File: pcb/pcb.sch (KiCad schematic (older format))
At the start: 42 parts, among them CN1 USBA_FEMALE, CN4 MicroUSB, T1 MMUN2133LT1G, U1 TPS61090RSAR, U2 MCP73871, X1 TERMBLOCK_1X2

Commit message: excluding unused kicad files, added start of schematic with reference
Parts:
- removed FID1, FID2, FID3: FIDUCIAL\"\", pcb:FIDUCIAL_1MM, symbol pcb-eagle-import:FIDUCIAL""
- removed U$10, U$11: MOUNTINGHOLE2.5, pcb:MOUNTINGHOLE_2.5_PLATED, symbol pcb-eagle-import:MOUNTINGHOLE2.5
- added C1, C2: 10µF, lipousbc:0805-NO@1, symbol lipousbc-eagle-import:CAP_CERAMIC0805-NOOUTLINE
- added C?: 10 uF, symbol Device:C
- added CN2: JSTPH, lipousbc:JSTPH2, symbol lipousbc-eagle-import:JST_2PIN
- added D?: ORANGE_LED, symbol Device:LED
- added D?: GREEN_LED, symbol Device:LED
- added J?: B2B-PH-K-S_LF__SN_, digikey-footprints:PinHeader_1x2_P2mm_Drill1mm, symbol dk_Rectangular-Connectors-Headers-Male-Pins:B2B-PH-K-S_LF__SN_
- added J?: Conn_02x08_Odd_Even, Connector_PinHeader_2.54mm:PinHeader_2x08_P2.54mm_Vertical, symbol Connector_Generic:Conn_02x08_Odd_Even
- added JP4: HEADER-1X570MIL, lipousbc:1X05_ROUND_70, symbol lipousbc-eagle-import:HEADER-1X570MIL
- added LED1: RED, lipousbc:CHIPLED_0805_NOOUTLINE, symbol lipousbc-eagle-import:LED0805_NOOUTLINE
- added LED2: GREEN, lipousbc:CHIPLED_0805_NOOUTLINE, symbol lipousbc-eagle-import:LED0805_NOOUTLINE
- added R1, R2: 470, lipousbc:0603-NO, symbol lipousbc-eagle-import:RESISTOR_0603_NOOUT
- added R3: 10K\\, lipousbc:0603-NO, symbol lipousbc-eagle-import:RESISTOR_0603_NOOUT
- added R4: 2.2K, lipousbc:0603-NO, symbol lipousbc-eagle-import:RESISTOR_0603_NOOUT
- added R5, R6: 5.1K, lipousbc:0603-NO, symbol lipousbc-eagle-import:RESISTOR_0603_NOOUT
- added R? (x2): 5.1k, symbol Device:R
- added R?: 270K, symbol Device:R
- added R? (x2): 100K, symbol Device:R
- added R?: 1.0K, symbol Device:R
- added R? (x2): 1K, symbol Device:R
- added S?: GPTS203211B, digikey-footprints:PushButton_12x12mm_THT_GPTS203211B, symbol dk_Pushbutton-Switches:GPTS203211B
- added SJ1: SOLDERJUMPER, lipousbc:SOLDERJUMPER_ARROW_NOPASTE, symbol lipousbc-eagle-import:SOLDERJUMPER
- added TH?: 15K, symbol Device:Thermistor
- added U1: MCP73831T-2ACI/OT, lipousbc:SOT23-5, symbol lipousbc-eagle-import:MCP73831_2
- added U?: TPS61090, Package_DFN_QFN:Texas_S-PVQFN-N16_EP2.7x2.7mm_ThermalVias, symbol Regulator_Switching:TPS61090
- added U?: MCP73871-1AA, Package_DFN_QFN:QFN-20-1EP_4x4mm_P0.5mm_EP2.5x2.5mm, symbol Battery_Management:MCP73871-1AA
- added X2: USB_C, lipousbc:USB_C_CUSB31-CFM2AX-01-X, symbol lipousbc-eagle-import:USB_C
- added X?: USB_C, digikey-footprints:USB-C_Female_E8124-015-01, symbol lipousbc-eagle-import:USB_C
- B1: symbol pcb-eagle-import:BATTERY -> pcb-rescue:BATTERY-pcb-eagle-import
- C6: symbol pcb-eagle-import:C-USC1210 -> pcb-rescue:C-USC1210-pcb-eagle-import
- CN1: symbol pcb-eagle-import:USB_TYPEAPTHFML -> pcb-rescue:USB_TYPEAPTHFML-pcb-eagle-import
- CN4: symbol pcb-eagle-import:USBMICRO_20329 -> pcb-rescue:USBMICRO_20329-pcb-eagle-import
- JP2: symbol pcb-eagle-import:HEADER-1X8ROUND -> pcb-rescue:HEADER-1X8ROUND-pcb-eagle-import
- L1: symbol pcb-eagle-import:INDUCTORTDK_VLC5045 -> pcb-rescue:INDUCTORTDK_VLC5045-pcb-eagle-import
- T1: symbol pcb-eagle-import:-PNP_DRIVER-SC59-BEC -> pcb-rescue:-PNP_DRIVER-SC59-BEC-pcb-eagle-import
- U1: symbol pcb-eagle-import:VREG_TPS6103X -> pcb-rescue:VREG_TPS6103X-pcb-eagle-import
- U2: symbol pcb-eagle-import:MCP73871 -> pcb-rescue:MCP73871-pcb-eagle-import
- X1: symbol pcb-eagle-import:TERMBLOCK_1X2 -> pcb-rescue:TERMBLOCK_1X2-pcb-eagle-import
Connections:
- net labels added: 5V, CC1, CC2, D+, D-
- net labels removed: FRAME_A4_ADAFRUIT
- wire segments 129 -> 205
- no-connect marks 0 -> 5
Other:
- note added: "10K = 100mA"
- note added: "5.0K = 200mA"
- note added: "Input power over micro-USB"
- note added: "Output power over USB-A"
- note added: "REFERENCE: Adafruit Micro-Lipo Charger\n(https://github.com/adafruit/Adafruit-MicroLipo-PCB)"
- note added: "REFERENCE: Adafruit PowerBoost 1000C\n(https://github.com/adafruit/Adafruit-PowerBoost-1000C)"
- note added: "RPi header, first 16 pins (2x8)"
- note added: "Set to UFP (Peripheral)\nAlso marks this as a USB 2.0 peripheral device\n\nFor DFP (Host) you need pullups\nhere instead of pulldowns."
- note added: "Upstream/Downstream Facing Port Setup:"
- moved on the sheet: C1, C2, C4, C7, C8, CHRG/LBO1, DONE1, LED1, LED2, R1, R10, R11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

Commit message: added some more components
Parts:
- added C?: 10 uF, symbol Device:C
- added Q?: MMUN2211LT1G, digikey-footprints:SOT-23-3, symbol dk_Transistors-Bipolar-BJT-Single-Pre-Biased:MMUN2211LT1G
- C1, C2: symbol lipousbc-eagle-import:CAP_CERAMIC0805-NOOUTLINE -> pcb-rescue:CAP_CERAMIC0805-NOOUTLINE-lipousbc-eagle-import
- CN2: symbol lipousbc-eagle-import:JST_2PIN -> pcb-rescue:JST_2PIN-lipousbc-eagle-import
- JP4: symbol lipousbc-eagle-import:HEADER-1X570MIL -> pcb-rescue:HEADER-1X570MIL-lipousbc-eagle-import
- LED1, LED2: symbol lipousbc-eagle-import:LED0805_NOOUTLINE -> pcb-rescue:LED0805_NOOUTLINE-lipousbc-eagle-import
- R1, R2, R3, R4, R5, R6: symbol lipousbc-eagle-import:RESISTOR_0603_NOOUT -> pcb-rescue:RESISTOR_0603_NOOUT-lipousbc-eagle-import
- SJ1: symbol lipousbc-eagle-import:SOLDERJUMPER -> pcb-rescue:SOLDERJUMPER-lipousbc-eagle-import
- U1: symbol lipousbc-eagle-import:MCP73831_2 -> pcb-rescue:MCP73831_2-lipousbc-eagle-import
- X2, X?: symbol lipousbc-eagle-import:USB_C -> pcb-rescue:USB_C-lipousbc-eagle-import
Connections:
- net labels added: PI_3V3, PI_BCM_14_TXD, PI_BCM_15_RXD, PI_BCM_17, PI_BCM_18_PWM0, PI_BCM_22, PI_BCM_23, PI_BCM_27, PI_BCM_2_SDA, PI_BCM_3_SCL, PI_BCM_4_GPCLK0
- wire segments 205 -> 212
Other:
- moved on the sheet: J?, S?

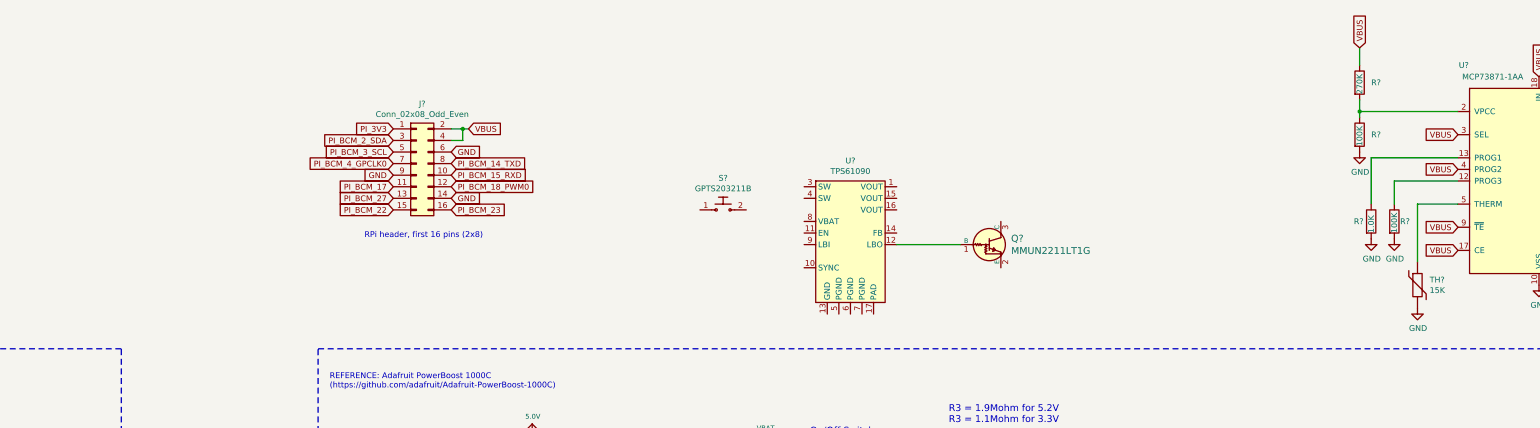
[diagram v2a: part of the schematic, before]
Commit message: first pass of schematic complete
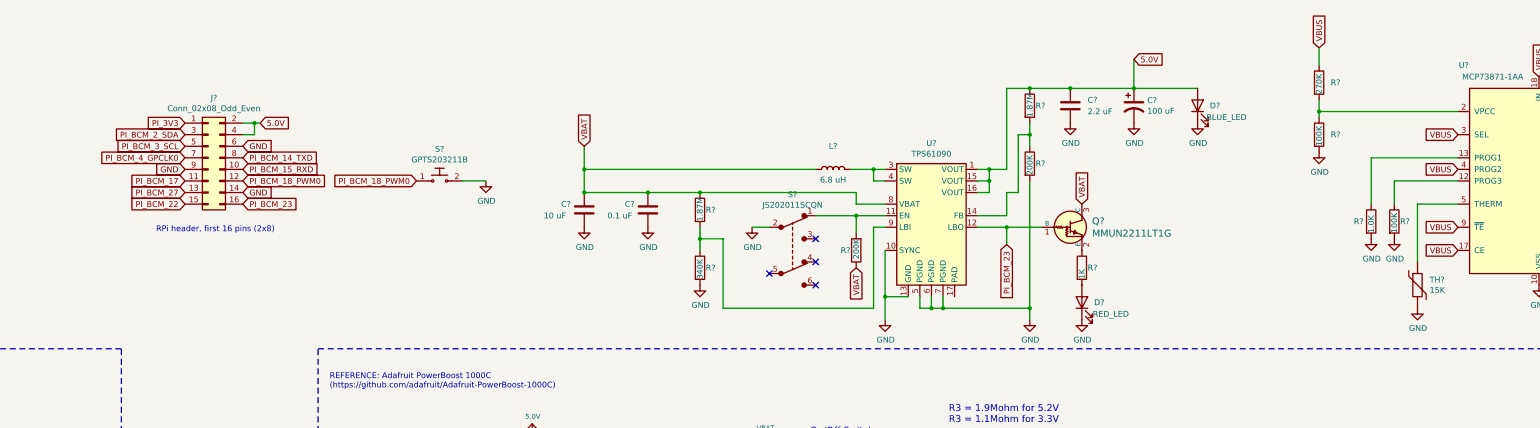
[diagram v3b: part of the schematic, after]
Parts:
- added C?: 2.2 uF, symbol Device:C
- added C?: 100 uF, symbol Device:CP1
- added C?: 10 uF, symbol Device:C
- added C?: 0.1 uF, symbol Device:C
- added D?: RED_LED, symbol Device:LED
- added D?: BLUE_LED, symbol Device:LED
- added L?: 6.8 uH, symbol Device:L
- added R? (x2): 200K, symbol Device:R
- added R?: 1K, symbol Device:R
- added R? (x2): 1.87M, symbol Device:R
- added R?: 340K, symbol Device:R
- added S?: JS202011SCQN, Button_Switch_THT:SW_CuK_JS202011AQN_DPDT_Angled, symbol dk_Slide-Switches:JS202011SCQN
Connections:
- net 5.0V: now also J?.2 (Pin_2), J?.4 (Pin_4), U?.1 (VOUT), U?.15 (VOUT), U?.16 (VOUT), C?.1, C?.1, D?.2 (A), R?.1
- net GND: now also S?.2, U?.10 (SYNC), U?.13 (GND), U?.5 (PGND), U?.6 (PGND), U?.7 (PGND), C?.2, C?.2, C?.2, C?.2, D?.1 (K), D?.1 (K), R?.2, R?.2, S?.2
- net PI_BCM_18_PWM0: now also S?.1
- net PI_BCM_23: now also Q?.1 (B), U?.12 (LBO)
- net VBAT: now also Q?.3 (C), U?.8 (VBAT), C?.1, C?.1, L?.1, R?.1, R?.1
- net VBUS: no longer J?.2 (Pin_2), J?.4 (Pin_4)
- net at Q?.2 (E): now also R?.1
- net at U?.11 (EN): now also R?.2, S?.1
- net at U?.14 (FB): now also R?.1, R?.2
- net at U?.3 (SW): now also U?.4 (SW), L?.2
- net at U?.9 (LBI): now also R?.1, R?.2
- new net: D?.2 (A), R?.2
- no-connect marks 5 -> 9
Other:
- moved on the sheet: J?, Q?, R?, S?, U?

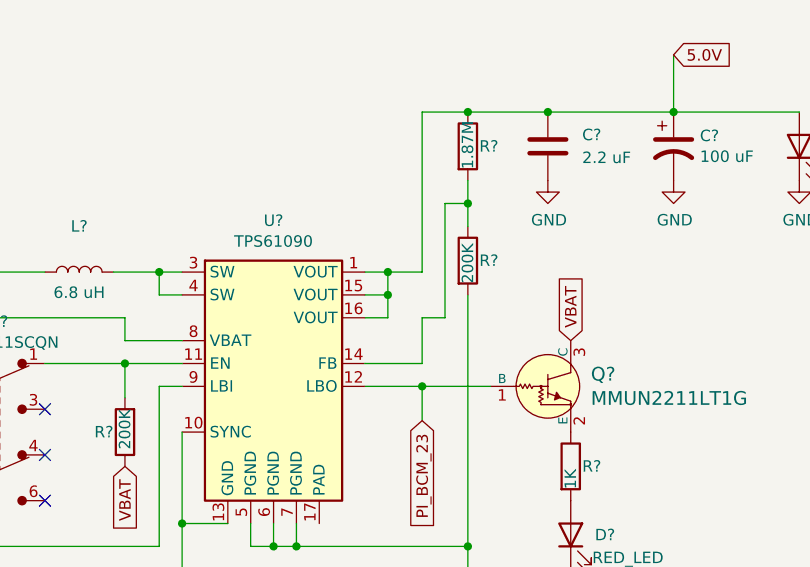
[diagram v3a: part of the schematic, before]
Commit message: updated schematic a bit, going to delete reference
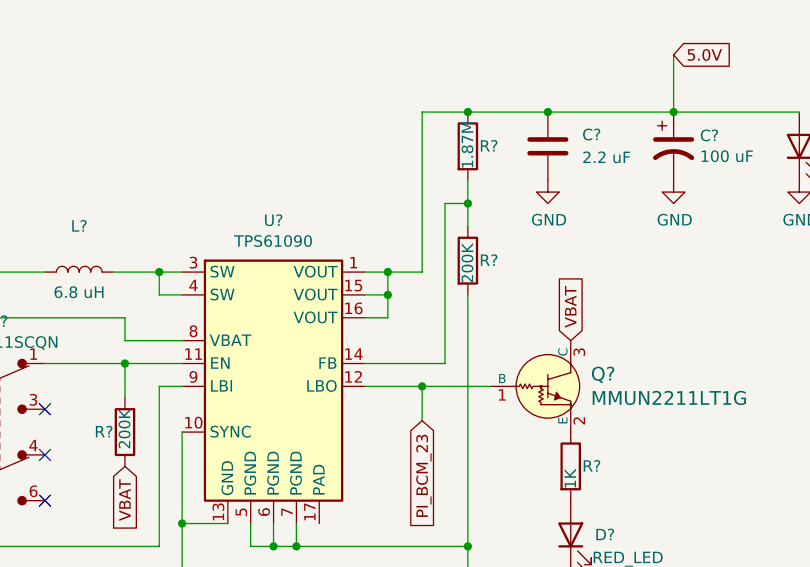
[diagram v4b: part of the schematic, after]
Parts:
- C? (x3): footprint (none) -> Capacitor_SMD:C_0805_2012Metric
- C?: footprint (none) -> Capacitor_SMD:C_0201_0603Metric
- C?: footprint (none) -> Capacitor_SMD:C_1206_3216Metric
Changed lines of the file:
@@
 F 0 "C?" H 9050 10900 50  0000 L CNN
 F 1 "10 uF" H 8950 10800 50  0000 L CNN
-F 2 "" H 9338 10650 50  0001 C CNN
+F 2 "Capacitor_SMD:C_0805_2012Metric" H 9338 10650 50  0001 C CNN
 F 3 "~" H 9300 10800 50  0001 C CNN
 	1    9300 10800
@@
 F 0 "C?" H 25950 11150 50  0000 L CNN
 F 1 "10 uF" H 25850 11050 50  0000 L CNN
-F 2 "" H 26238 10900 50  0001 C CNN
+F 2 "Capacitor_SMD:C_0805_2012Metric" H 26238 10900 50  0001 C CNN
 F 3 "~" H 26200 11050 50  0001 C CNN
 	1    26200 11050
@@
 	19200 11200 19300 11200
 Wire Wire Line
-	20100 11500 20350 11500
-Wire Wire Line
-	20350 11500 20350 11300
-Wire Wire Line
 	20200 11100 20200 11200
 Wire Wire Line
@@
 	20350 10400 20550 10400
 Wire Wire Line
-	20350 11300 20450 11300
-Wire Wire Line
-	20450 11300 20450 10800
-Wire Wire Line
 	20450 10800 20550 10800
 Wire Wire Line
@@
 F 0 "C?" H 21050 10600 50  0000 L CNN
 F 1 "2.2 uF" H 21050 10500 50  0000 L CNN
-F 2 "" H 20938 10400 50  0001 C CNN
-F 3 "~" H 20900 10550 50  0001 C CNN
+F 2 "Capacitor_SMD:C_0201_0603Metric" H 20938 10400 50  0001 C CNN
+F 3 "https://www.digikey.com/product-detail/en/C0603C225M9PAC7867/399-13137-1-ND/5879291/?itemSeq=336152622" H 20900 10550 50  0001 C CNN
 	1    20900 10550
 	1    0    0    -1
@@
 F 0 "C?" H 21565 10596 50  0000 L CNN
 F 1 "100 uF" H 21565 10505 50  0000 L CNN
-F 2 "" H 21450 10550 50  0001 C CNN
-F 3 "~" H 21450 10550 50  0001 C CNN
+F 2 "Capacitor_SMD:C_1206_3216Metric" H 21450 10550 50  0001 C CNN
+F 3 "https://www.digikey.com/product-detail/en/kemet/C1206C107M9PACTU/399-5620-1-ND/2057834" H 21450 10550 50  0001 C CNN
 	1    21450 10550
 	1    0    0    -1
@@
 F 0 "C?" H 16500 11500 50  0000 L CNN
 F 1 "10 uF" H 16350 11400 50  0000 L CNN
-F 2 "" H 16738 11300 50  0001 C CNN
+F 2 "Capacitor_SMD:C_0805_2012Metric" H 16738 11300 50  0001 C CNN
 F 3 "~" H 16700 11450 50  0001 C CNN
 	1    16700 11450
@@
 Wire Wire Line
 	23050 10600 24250 10600
+Wire Wire Line
+	20100 11500 20450 11500
+Wire Wire Line
+	20450 10800 20450 11500
 $EndSCHEMATC

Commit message: netlist has a bug it seems
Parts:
- removed B1: JST 2-PH, pcb:JSTPH2, symbol pcb-rescue:BATTERY-pcb-eagle-import
- removed C1, C2: 10µF, lipousbc:0805-NO@1, symbol pcb-rescue:CAP_CERAMIC0805-NOOUTLINE-lipousbc-eagle-import
- removed C1, C7, C8: 10uF, pcb:0805-NO, symbol pcb-eagle-import:CAP_CERAMIC0805-NOOUTLINE
- removed C2: 2.2uF, pcb:0805-NO, symbol pcb-eagle-import:CAP_CERAMIC0805-NOOUTLINE
- removed C4: 0.1uF, pcb:0805_10MGAP, symbol pcb-eagle-import:CAP_CERAMIC0805_10MGAP
- removed C6: 100uF, pcb:C1210, symbol pcb-rescue:C-USC1210-pcb-eagle-import
- removed CHRG/LBO1: ORANGE, pcb:CHIPLED_0805_NOOUTLINE, symbol pcb-eagle-import:LED0805_NOOUTLINE
- removed CN1: USBA_FEMALE, pcb:USB_HOST-PTH, symbol pcb-rescue:USB_TYPEAPTHFML-pcb-eagle-import
- removed CN2: JSTPH, lipousbc:JSTPH2, symbol pcb-rescue:JST_2PIN-lipousbc-eagle-import
- removed CN4: MicroUSB, pcb:4UCONN_20329, symbol pcb-rescue:USBMICRO_20329-pcb-eagle-import
- removed DONE1: GREEN, pcb:CHIPLED_0805_NOOUTLINE, symbol pcb-eagle-import:LED0805_NOOUTLINE
- removed JP2: HEADER-1X8ROUND, pcb:1X08_ROUND, symbol pcb-rescue:HEADER-1X8ROUND-pcb-eagle-import
- removed JP4: HEADER-1X570MIL, lipousbc:1X05_ROUND_70, symbol pcb-rescue:HEADER-1X570MIL-lipousbc-eagle-import
- removed L1: 6.8uH, pcb:INDUCTOR_5X5MM_TDK_VLC5045, symbol pcb-rescue:INDUCTORTDK_VLC5045-pcb-eagle-import
- removed LED1: RED, lipousbc:CHIPLED_0805_NOOUTLINE, symbol pcb-rescue:LED0805_NOOUTLINE-lipousbc-eagle-import
- removed LED1: RED, pcb:CHIPLED_0805_NOOUTLINE, symbol pcb-eagle-import:LED0805_NOOUTLINE
- removed LED2: GREEN, lipousbc:CHIPLED_0805_NOOUTLINE, symbol pcb-rescue:LED0805_NOOUTLINE-lipousbc-eagle-import
- removed LED2: BLUE, pcb:CHIPLED_0805_NOOUTLINE, symbol pcb-eagle-import:LED0805_NOOUTLINE
- removed R1, R2: 470, lipousbc:0603-NO, symbol pcb-rescue:RESISTOR_0603_NOOUT-lipousbc-eagle-import
- removed R1: 1.87M, pcb:_0805MP, symbol pcb-eagle-import:RESISTOR_0805MP
- removed R10: 49.9K, pcb:0805-NO, symbol pcb-eagle-import:RESISTOR0805_NOOUTLINE
- removed R11: 75K 1%, pcb:0805-NO, symbol pcb-eagle-import:RESISTOR0805_NOOUTLINE
- removed R12: 49.9K 1%, pcb:0805-NO, symbol pcb-eagle-import:RESISTOR0805_NOOUTLINE
- removed R13, R4: 200K, pcb:0805-NO, symbol pcb-eagle-import:RESISTOR0805_NOOUTLINE
- removed R14, R20, R5, R8: 1K, pcb:0805-NO, symbol pcb-eagle-import:RESISTOR0805_NOOUTLINE
- removed R16: 1.0K, pcb:0805-NO, symbol pcb-eagle-import:RESISTOR0805_NOOUTLINE
- removed R17, R7: 100K, pcb:0805-NO, symbol pcb-eagle-import:RESISTOR0805_NOOUTLINE
- removed R2: 340K, pcb:_0805MP, symbol pcb-eagle-import:RESISTOR_0805MP
- removed R3: 1.87M, pcb:0805-NO, symbol pcb-eagle-import:RESISTOR0805_NOOUTLINE
- removed R3: 10K\\, lipousbc:0603-NO, symbol pcb-rescue:RESISTOR_0603_NOOUT-lipousbc-eagle-import
- removed R4: 2.2K, lipousbc:0603-NO, symbol pcb-rescue:RESISTOR_0603_NOOUT-lipousbc-eagle-import
- removed R5, R6: 5.1K, lipousbc:0603-NO, symbol pcb-rescue:RESISTOR_0603_NOOUT-lipousbc-eagle-import
- removed R6: 270K, pcb:0805-NO, symbol pcb-eagle-import:RESISTOR0805_NOOUTLINE
- removed R9: 43K, pcb:0805-NO, symbol pcb-eagle-import:RESISTOR0805_NOOUTLINE
- removed S?: GPTS203211B, digikey-footprints:PushButton_12x12mm_THT_GPTS203211B, symbol dk_Pushbutton-Switches:GPTS203211B
- removed SJ1: SOLDERJUMPER, lipousbc:SOLDERJUMPER_ARROW_NOPASTE, symbol pcb-rescue:SOLDERJUMPER-lipousbc-eagle-import
- removed T1: MMUN2133LT1G, pcb:SC59-BEC, symbol pcb-rescue:-PNP_DRIVER-SC59-BEC-pcb-eagle-import
- removed TH?: 15K, symbol Device:Thermistor
- removed THERM1: 15K, pcb:0805-NO, symbol pcb-eagle-import:RESISTOR0805_NOOUTLINE
- removed U1: TPS61090RSAR, pcb:PVQFN-16, symbol pcb-rescue:VREG_TPS6103X-pcb-eagle-import
- removed U1: MCP73831T-2ACI/OT, lipousbc:SOT23-5, symbol pcb-rescue:MCP73831_2-lipousbc-eagle-import
- removed U2: MCP73871, pcb:QFN20_4MM, symbol pcb-rescue:MCP73871-pcb-eagle-import
- removed X1: TERMBLOCK_1X2, pcb:TERMBLOCK_1X2-3.5MM, symbol pcb-rescue:TERMBLOCK_1X2-pcb-eagle-import
- removed X2: USB_C, lipousbc:USB_C_CUSB31-CFM2AX-01-X, symbol pcb-rescue:USB_C-lipousbc-eagle-import
- added R15: 15K, Resistor_SMD:R_0402_1005Metric, symbol Device:R
- added SW1: SW_SPST, tinycam:FP11SPA1B1TP00, symbol Switch:SW_SPST
- C2: renamed from C?; footprint (none) -> Capacitor_SMD:C_01005_0402Metric
- D1, D2, D3, D4: renamed from D?; footprint (none) -> LED_SMD:LED_0805_2012Metric
- L1: renamed from L?; footprint (none) -> Inductor_SMD:L_Wuerth_HCI-5040
- R1, R10, R12, R13, R14, R2, R3, R4, R5, R6, R7, R8: renamed from R?; footprint (none) -> Resistor_SMD:R_0402_1005Metric
- R11: renamed from R?; value 1.0K -> 1K; footprint (none) -> Resistor_SMD:R_0402_1005Metric
- R9: renamed from R?; footprint (none) -> Resistor_SMD:R_0201_0603Metric
- gave numbers to parts that had none: 12
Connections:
- net GND: now also R15.2, SW1.2 (B)
- net PI_BCM_18_PWM0: now also SW1.1 (A)
- net at U2.5 (THERM): now also R15.1
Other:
- note removed: "1.0K = 1000mA"
- note removed: "10K = 100mA"
- note removed: "10K NTC Thermistor:"
- note removed: "2.0K = 500mA"
- note removed: "5.0K = 200mA"
- note removed: "6.8uH power\nw/2A current"
- note removed: "Both grounds must be connected on the PCB at only one point close to the GND pin."
- note removed: "Charge Rate = 1000V/PROG1"
- note removed: "Input power over micro-USB"
- note removed: "No Thermistor:"
- note removed: "On/Off Switch"
- note removed: "Output power over USB-A"
- note removed: "R3 = 1.9Mohm for 5.2V\nR3 = 1.1Mohm for 3.3V"
- note removed: "REFERENCE: Adafruit Micro-Lipo Charger\n(https://github.com/adafruit/Adafruit-MicroLipo-PCB)"
- note removed: "REFERENCE: Adafruit PowerBoost 1000C\n(https://github.com/adafruit/Adafruit-PowerBoost-1000C)"
- note removed: "RT1 = 0, RT2 = 10K"
- note removed: "RT1 = TBD, RT2 = TBD"
- note removed: "See Pg 15\n1st para"
- note removed: "Upstream/Downstream Facing Port Setup:"
- moved on the sheet: C1, C2, C3, C4, C5, C6, D1, D2, D3, D4, J1, J2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
